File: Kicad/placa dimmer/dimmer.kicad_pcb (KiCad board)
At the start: 2 copper layers, 100 x 100 mm, 53 parts, among them J1 Screw_Terminal_01x02, J2 Screw_Terminal_01x02, J3 Screw_Terminal_01x02, J4 Conn_01x05_Socket, Q1 2N7000, Q2 2N7000, U1 MOC3023M, U2 4N25, U3 74HC14, U4 MOC3023M

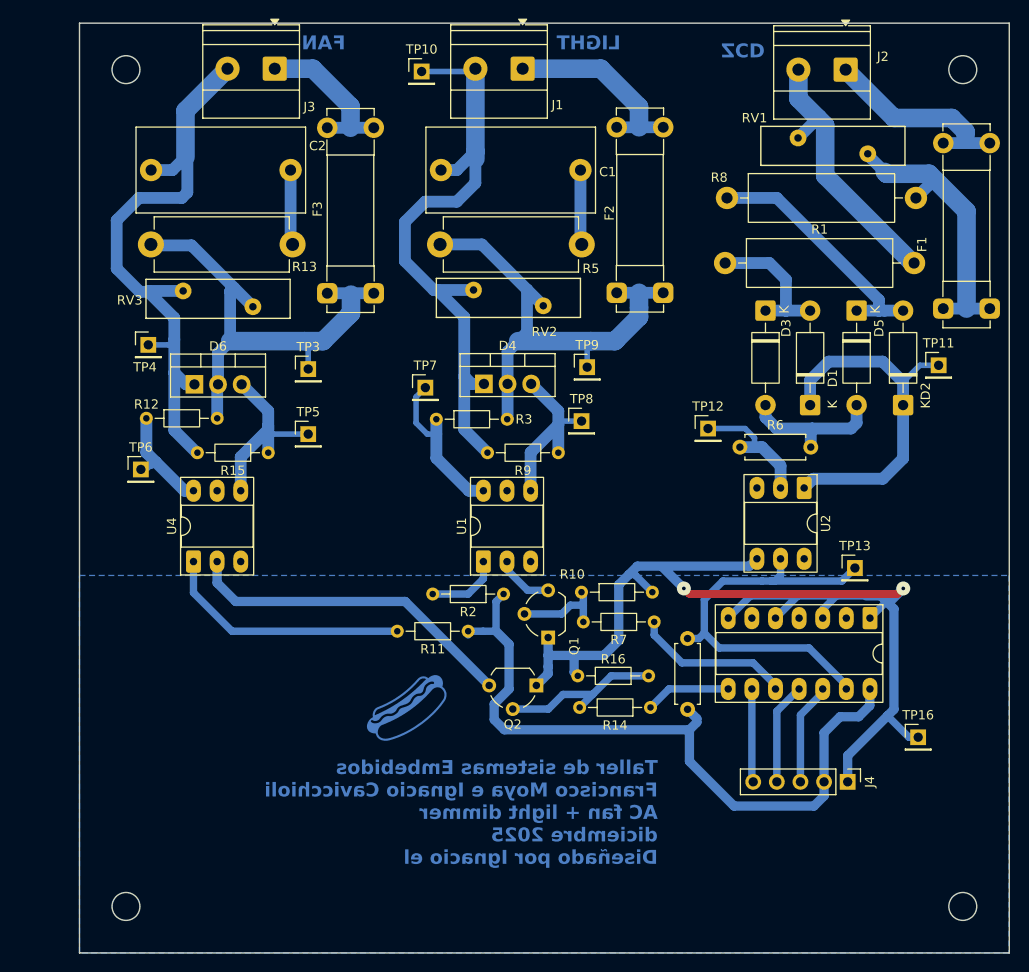
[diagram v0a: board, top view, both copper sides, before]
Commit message: arreglos
arreglos comentados en el pull request
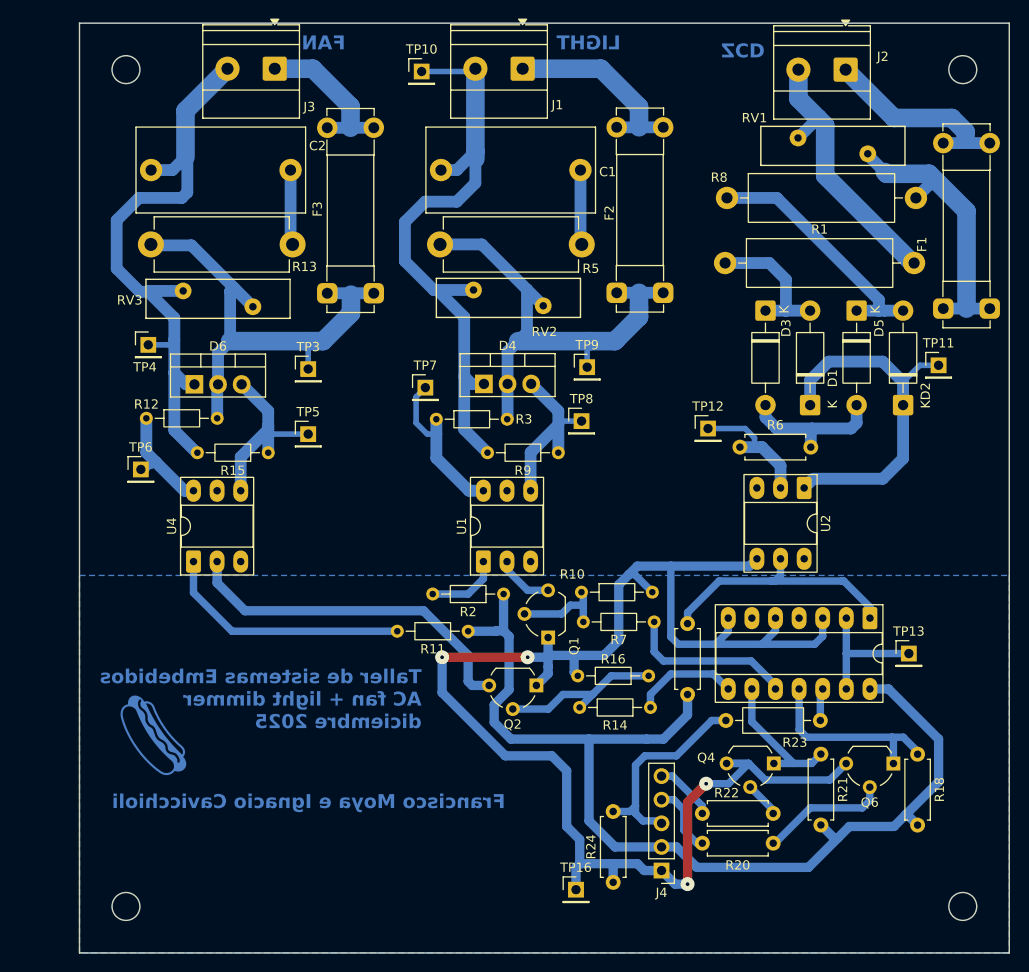
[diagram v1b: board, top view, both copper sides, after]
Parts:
- added Q4: NPN, Package_TO_SOT_THT:TO-92_Wide, F.Cu at (183.5, 131.2)
- added Q6: NPN, Package_TO_SOT_THT:TO-92_Wide, F.Cu at (196.3, 131.2)
- added R18: 2k2, Resistor_THT:R_Axial_DIN0207_L6.3mm_D2.5mm_P7.62mm_Horizontal, F.Cu at (198.9, 130.2)
- added R20: 2k2, Resistor_THT:R_Axial_DIN0207_L6.3mm_D2.5mm_P7.62mm_Horizontal, F.Cu at (183.4, 139.8)
- added R21: 2k2, Resistor_THT:R_Axial_DIN0207_L6.3mm_D2.5mm_P7.62mm_Horizontal, F.Cu at (188.5, 130.2)
- added R22: 2k2, Resistor_THT:R_Axial_DIN0207_L6.3mm_D2.5mm_P7.62mm_Horizontal, F.Cu at (183.4, 136.6)
- added R23: 1k, Resistor_THT:R_Axial_DIN0207_L6.3mm_D2.5mm_P10.16mm_Horizontal, F.Cu at (188.5, 126.6)
- added R24: 2k2, Resistor_THT:R_Axial_DIN0207_L6.3mm_D2.5mm_P7.62mm_Horizontal, F.Cu at (166.2, 144.0)
- R6: value 2k -> 2k2
- U3: value 74HC14 -> CD40106
- moved TP16 40.3 mm to (162.2, 144.8)
- moved G*** 27.8 mm to (116.6, 128.4), turned to 125 degrees
- moved J4 22.2 mm to (171.4, 142.7), turned to 180 degrees
- moved TP13 10.9 mm to (198.0, 119.4)
- moved R4 1.60 mm to (174.2, 123.8)
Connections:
- J4 pad 4: /LIGHT -> /LIGHT_3V
- J4 pad 5: /FAN -> /FAN_3V
- TP13 pad 1: Net-(R4-Pad2) -> Net-(TP13-Pad1)
- U3 pad 1: GND -> Net-(R4-Pad2)
- U3 pad 12: /ZCD -> Net-(R23-Pad1)
- U3 pad 13: Net-(R4-Pad2) -> Net-(TP13-Pad1)
- U3 pad 2: unconnected-(U3-Pad2) -> Net-(TP13-Pad1)
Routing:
- net GND: track 124.6 -> 169.0 mm, vias 2 -> 4
- net +5V: track 77.9 -> 114.5 mm
- net Net-(R4-Pad2): track 44.3 -> 27.6 mm
- net Net-(TP13-Pad1): track 0.00 -> 14.3 mm
- net Net-(Q6-B): track 0.00 -> 13.7 mm
- net /ZCD: track 11.0 -> 22.8 mm
- net /LIGHT: track 11.0 -> 21.3 mm
- net /LIGHT_3V: track 0.00 -> 8.03 mm
- net /FAN_3V: track 0.00 -> 6.53 mm
- net /FAN: track 10.2 -> 15.5 mm
- net Net-(R23-Pad1): track 0.00 -> 3.90 mm
- net Net-(Q4-B): track 0.00 -> 3.86 mm
- net Net-(R14-Pad1): track 9.20 -> 11.3 mm
- net Net-(Q2-D): track 36.1 -> 37.8 mm
- net Net-(R7-Pad1): track 17.1 -> 18.1 mm
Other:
- board text added: "Francisco Moya e Ignacio Cavicchioli"
- board text added: "Taller de sistemas Embebidos AC fan + light dimmer diciembre 2025"
- board text removed: "Taller de sistemas Embebidos Francisco Moya e Ignacio Cavicchioli AC fan + light dimmer diciembre 2025 Diseñado por Ignacio el"

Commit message: previo a fabricación
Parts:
- added ?: , , F.Cu at (113.8, 146.6)
- added ?: , , F.Cu at (113.8, 56.6)
- added ?: , , F.Cu at (203.8, 56.6)
- added ?: , , F.Cu at (203.8, 146.6)
